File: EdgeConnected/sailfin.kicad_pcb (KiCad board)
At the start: 2 copper layers, 95.5 x 93 mm, 191 parts, among them J1 AnalogIn, J19 Barrel_Jack_Switch, J2 ATO1, J3 Raspberry_Pi_2_3, J4 Conn_02x25_Odd_Even, J5 i2c, J6 Screw_Terminal_01x02, J7 1wire, J8 PwmOut, J9 AnalogOut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

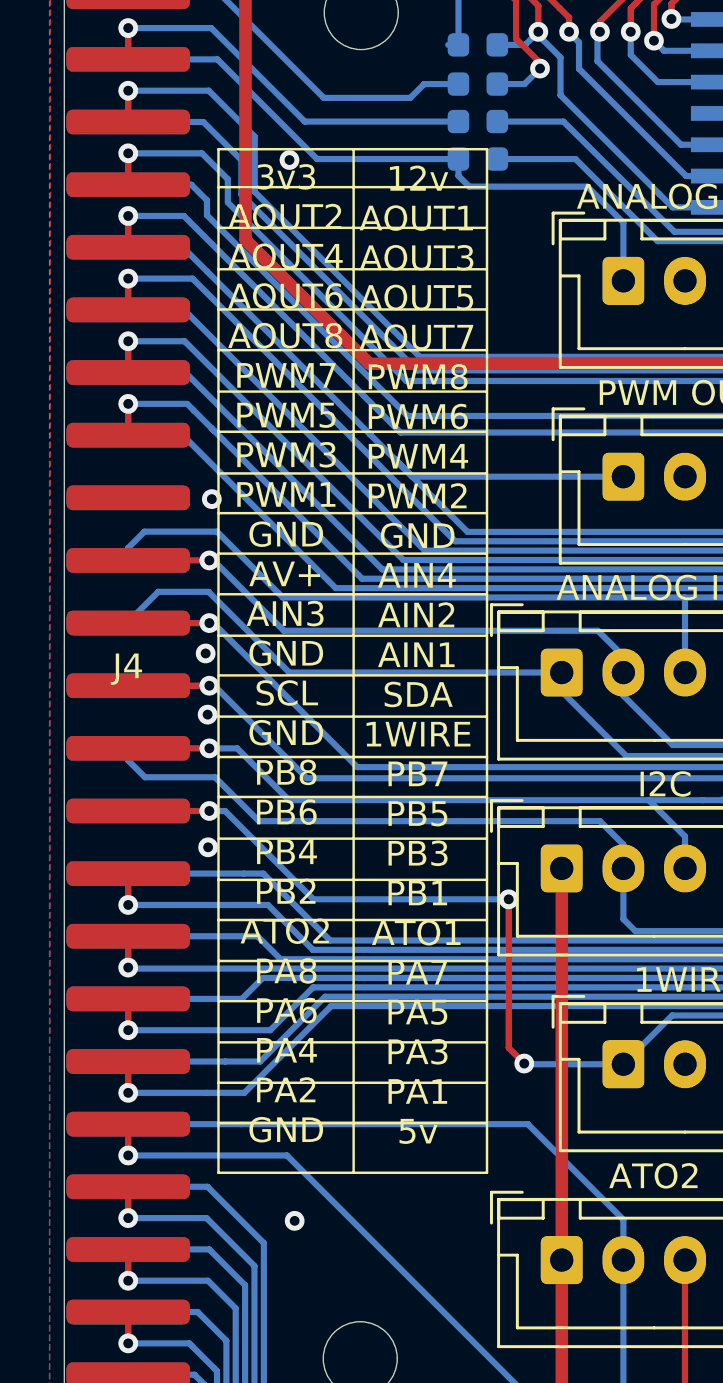
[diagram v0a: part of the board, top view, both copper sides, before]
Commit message: card edge revision
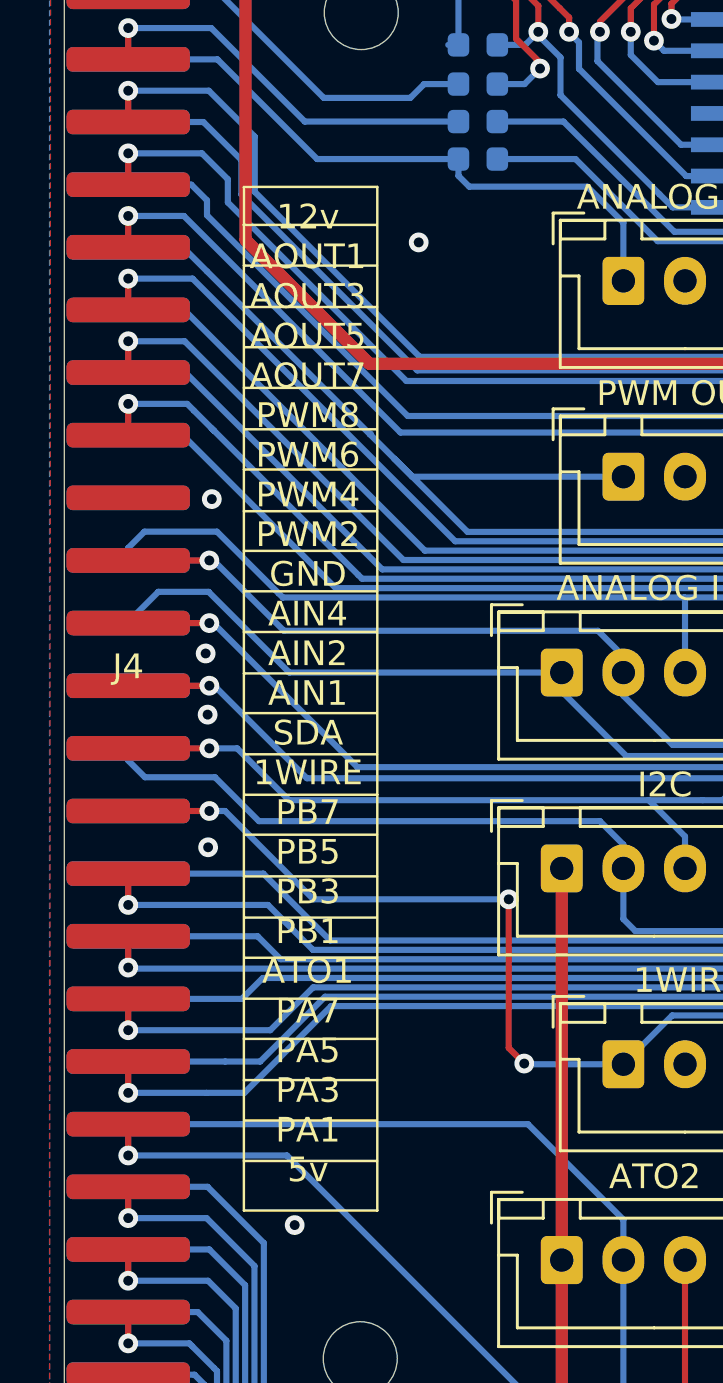
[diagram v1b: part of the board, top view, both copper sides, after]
